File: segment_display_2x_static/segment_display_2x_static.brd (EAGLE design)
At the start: 40 x 26 mm, 12 parts, among them IC1 74HC595D, IC2 74HC595D

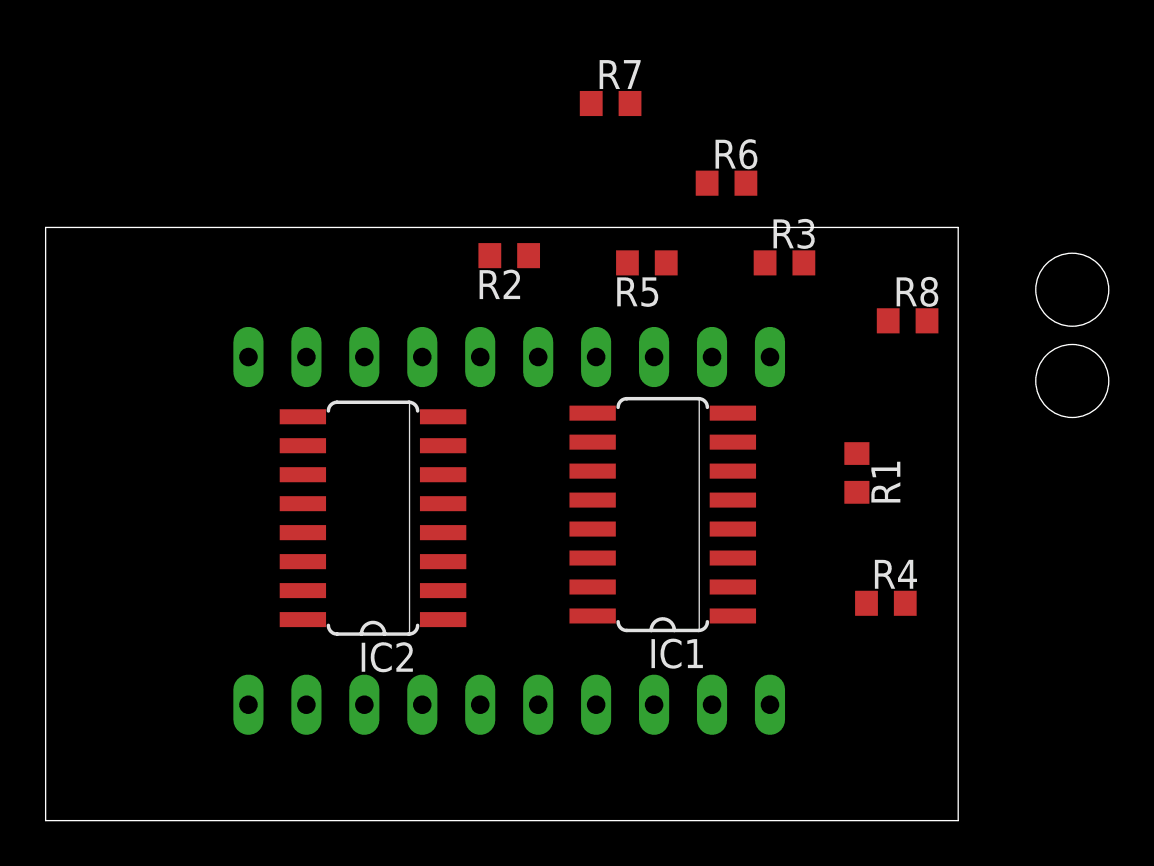
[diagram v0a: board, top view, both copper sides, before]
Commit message: added segment_display_2x_static
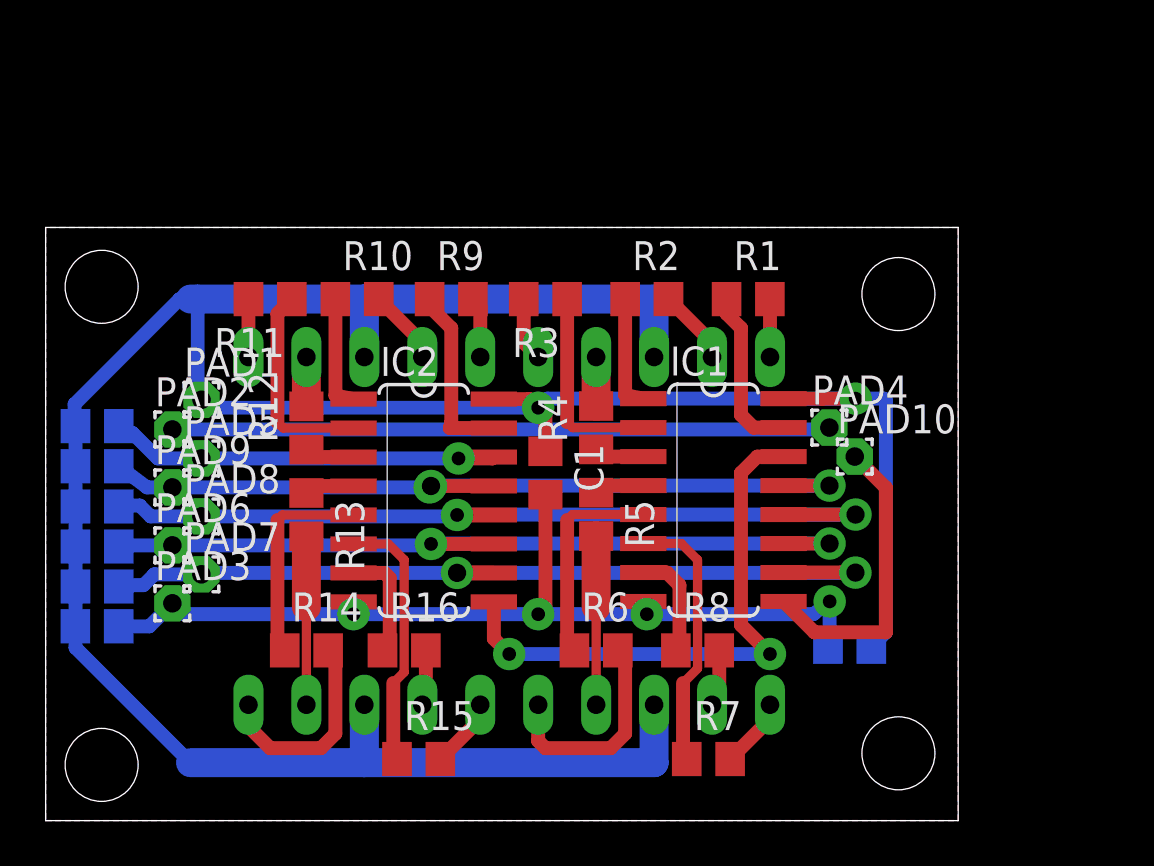
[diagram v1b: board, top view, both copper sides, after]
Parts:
- added C1, C2, C3: 0.1, rcl:C0805
- added PAD1, PAD10, PAD2, PAD3, PAD4, PAD5, PAD6, PAD7, PAD8, PAD9: (no value), wirepad:1,6/0,8
- added R10, R11, R12, R13, R14, R15, R16, R17, R18, R19, R20, R21, R9: (no value), rcl:R0805
- R1, R2, R3, R4, R5, R6, R7, R8: device rcl:R0603 -> rcl:R0805
- moved R7 29.1 mm to (29.1, 2.70)
- moved R6 21.3 mm to (24.1, 7.46)
- moved R8 17.1 mm to (28.6, 7.46)
- moved R4 14.8 mm to (24.1, 17.2), turned to 90 degrees
- moved R5 11.2 mm to (24.1, 13.4), turned to 270 degrees
- moved R3 10.6 mm to (21.9, 22.9), turned to 180 degrees
- moved R1 8.99 mm to (30.8, 22.9), turned to 0 degrees
- moved R2 6.33 mm to (26.4, 22.9), turned to 0 degrees
- moved IC2 2.35 mm to (16.6, 14.0), turned to 270 degrees
- moved IC1 2.31 mm to (29.3, 14.1), turned to 270 degrees
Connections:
- new net LINK: IC1.14, IC2.9
- new net OA2: DIS2.7, R12.2
- new net OB2: DIS2.6, R11.2
- new net OC2: DIS2.4, R13.2
- new net OD2: DIS2.2, R16.2
- new net OE: IC1.13, IC2.13, PAD9.1, R21.1
- new net OE2: DIS2.1, R15.2
- new net OF2: DIS2.9, R10.2
- new net OG2: DIS2.10, R9.2
- new net OH2: DIS2.5, R14.2
- new net QA2: IC2.15, R9.1
- new net QB2: IC2.1, R10.1
- new net QC2: IC2.2, R11.1
- new net QD2: IC2.3, R12.1
- new net QE2: IC2.4, R13.1
- new net QF2: IC2.5, R14.1
- new net QG2: IC2.6, R15.1
- new net QH2: IC2.7, R16.1
- new net RCK: IC1.12, IC2.12, PAD8.1, R20.1
- new net RET: PAD2.1, PAD4.1
- new net SCK: IC1.11, IC2.11, PAD6.1, R18.1
- new net SCL: IC1.10, IC2.10, PAD7.1, R19.1
- new net SIN: IC2.14, PAD5.1, R17.1
- new net SOUT: IC1.9, PAD10.1
- net GND: now also C1.2, C2.2, C3.2, PAD3.1
- net OA1: now also R4.2; no longer R1.2
- net OB1: now also R3.2; no longer R2.2
- net OC1: now also R5.2; no longer R3.2
- net OD1: now also R8.2; no longer R4.2
- net OE1: now also R7.2; no longer R5.2
- net OF1: now also R2.2; no longer R6.2
- net OG1: now also R1.2; no longer R7.2
- net OH1: now also R6.2; no longer R8.2
- net VCC: now also C1.1, C2.1, C3.1, DIS1.3, DIS1.8, DIS2.3, DIS2.8, PAD1.1, R17.2, R18.2, R19.2, R20.2, R21.2
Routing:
- net VCC: track 0.00 -> 129.4 mm, vias 0 -> 2
- net GND: track 0.00 -> 40.7 mm, vias 0 -> 4
- net SCL: track 0.00 -> 37.3 mm, vias 0 -> 2
- net RCK: track 0.00 -> 37.3 mm, vias 0 -> 2
- net OE: track 0.00 -> 36.3 mm, vias 0 -> 3
- net SCK: track 0.00 -> 36.0 mm, vias 0 -> 2
- net RET: track 0.00 -> 28.8 mm
- net LINK: track 0.00 -> 24.6 mm, vias 0 -> 2
- net SIN: track 0.00 -> 17.1 mm, vias 0 -> 1
- net SOUT: track 0.00 -> 13.3 mm
- net QG1: track 0.00 -> 11.7 mm
- net QG2: track 0.00 -> 11.5 mm
- net OH1: track 0.00 -> 9.58 mm
- net QF1: track 0.00 -> 9.29 mm
- net QF2: track 0.00 -> 9.28 mm
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- added copper zone on layer 1, net GND
- added copper zone on layer 16, net GND
